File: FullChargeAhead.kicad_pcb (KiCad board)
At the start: 2 copper layers, 16 parts, among them P101 USB_OTG, P102 CONN_01X02, P103 JST_2PIN, U101 MCP73834

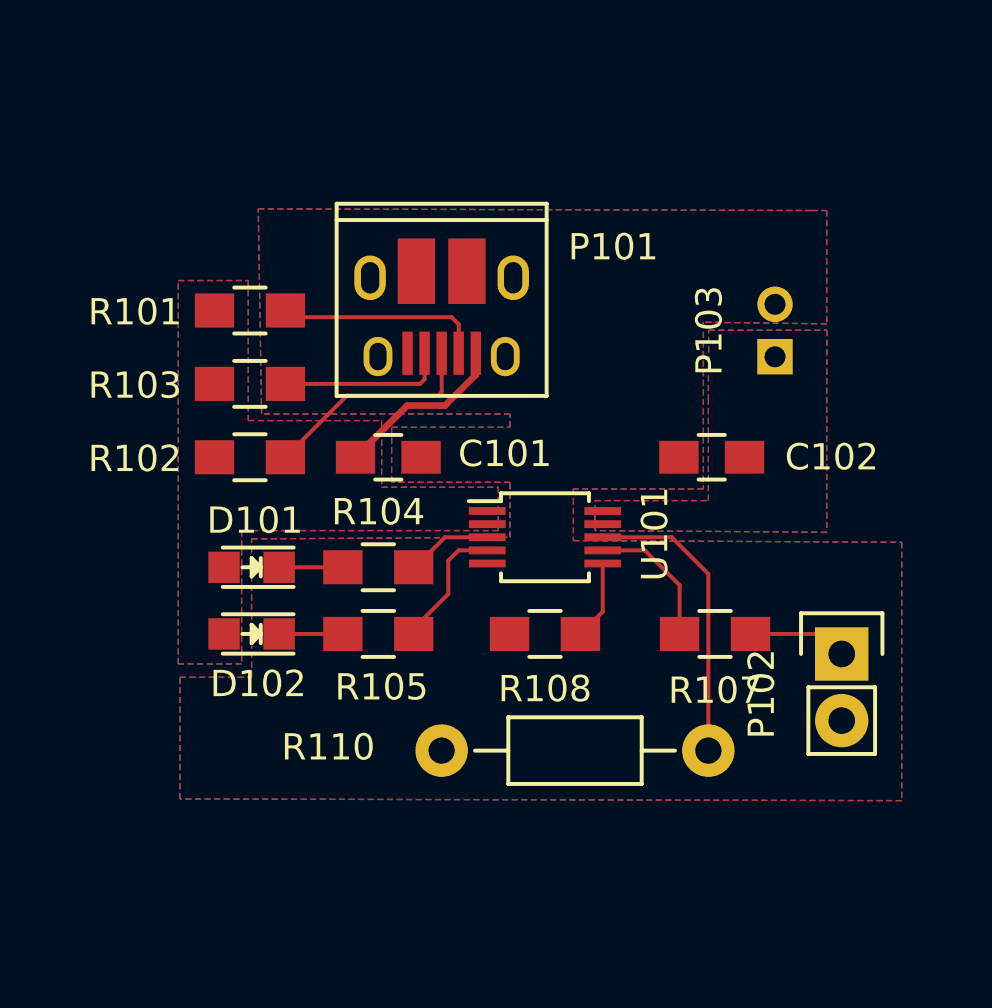
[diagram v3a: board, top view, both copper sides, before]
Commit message: new usb connector, via stiching, and gerbers
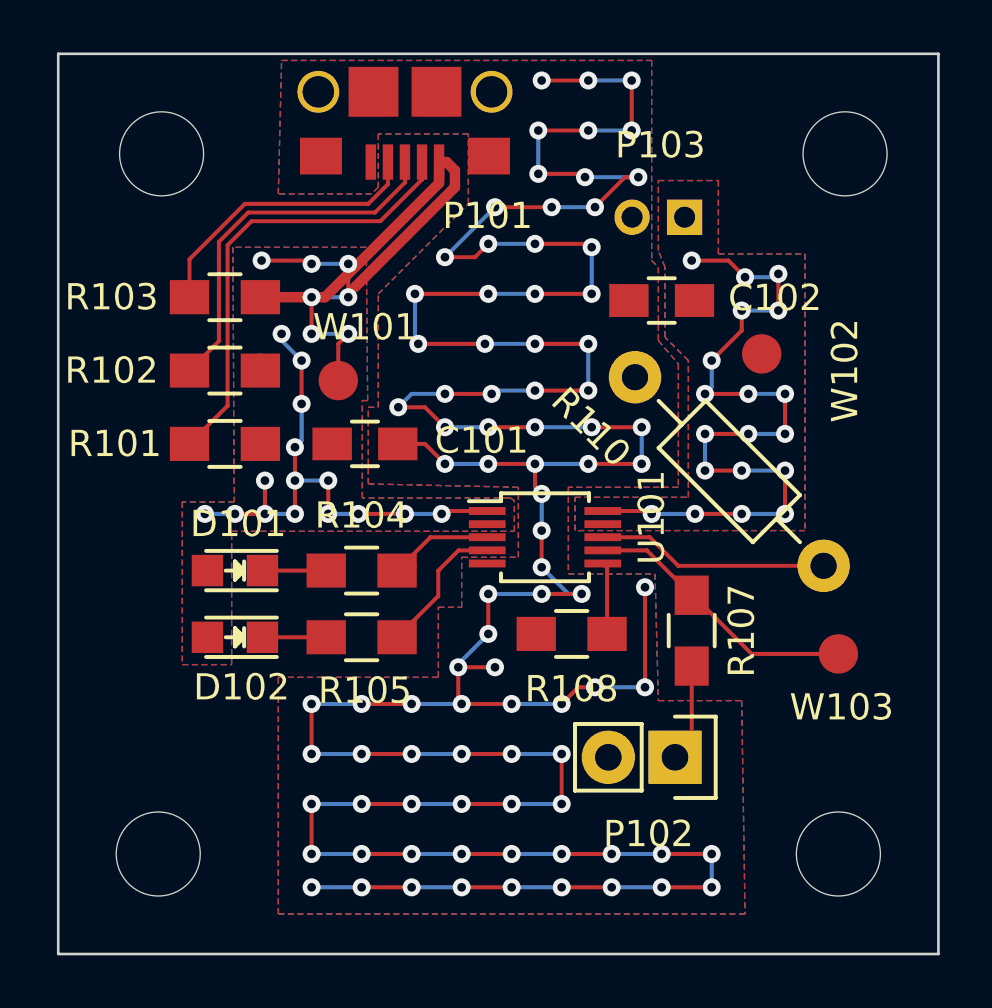
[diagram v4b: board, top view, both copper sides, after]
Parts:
- added REF**: MountingHole_3.2mm_M3, Mounting_Holes:MountingHole_3.2mm_M3, F.Cu at (164.8, 114.3)
- added REF**: MountingHole_3.2mm_M3, Mounting_Holes:MountingHole_3.2mm_M3, F.Cu at (138.9, 114.3)
- added REF**: MountingHole_3.2mm_M3, Mounting_Holes:MountingHole_3.2mm_M3, F.Cu at (139.1, 87.6)
- added REF**: MountingHole_3.2mm_M3, Mounting_Holes:MountingHole_3.2mm_M3, F.Cu at (165.1, 87.6)
- added W101: TEST_1P, Measurement_Points:Measurement_Point_Round-SMD-Pad_Small, F.Cu at (145.8, 96.3)
- added W102: TEST_1P, Measurement_Points:Measurement_Point_Round-SMD-Pad_Small, F.Cu at (161.9, 95.2)
- added W103: TEST_1P, Measurement_Points:Measurement_Point_Round-SMD-Pad_Small, F.Cu at (164.8, 106.7)
- P101: footprint FullChargeAhead:USB_Micro-B_10103594-0001LF -> FullChargeAhead:10118193
- moved R110 16.0 mm to (157.1, 96.1), turned to 315 degrees
- moved P101 8.57 mm to (148.3, 85.3)
- moved P102 7.47 mm to (158.6, 110.6), turned to 270 degrees
- moved C102 6.27 mm to (158.1, 93.2)
- moved P103 6.20 mm to (158.0, 90.0), turned to 0 degrees
- moved R101 5.17 mm to (141.5, 98.7), turned to 180 degrees
- moved R103 3.44 mm to (141.5, 93.1), turned to 180 degrees
- moved R102 3.44 mm to (141.5, 95.9), turned to 180 degrees
- moved C101 1.02 mm to (146.8, 98.7)
- moved R108 1.02 mm to (154.7, 105.9)
- moved R107 0.90 mm to (159.3, 105.8), turned to 270 degrees
- moved D101 0.65 mm to (141.9, 103.5)
- moved D102 0.65 mm to (141.9, 106.0)
- moved R104 0.65 mm to (146.7, 103.5)
- moved R105 0.65 mm to (146.7, 106.0)
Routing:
- net GND: track 0.00 -> 164.6 mm, vias 0 -> 87
- net /Vdd: track 6.70 -> 48.2 mm, vias 0 -> 22
- net /Vbat: track 0.00 -> 30.9 mm, vias 0 -> 19
- net Net-(P101-Pad2): track 7.92 -> 17.3 mm
- net Net-(P101-Pad3): track 8.46 -> 14.2 mm
- net Net-(R107-Pad1): track 5.33 -> 10.6 mm
- net Net-(P101-Pad4): track 6.37 -> 11.0 mm
- net Net-(R110-Pad2): track 11.3 -> 8.86 mm
- net Net-(R104-Pad2): track 3.27 -> 4.01 mm
- net Net-(R105-Pad2): track 4.98 -> 5.58 mm
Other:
- board outline added: 33.5 x 34.3 mm

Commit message: generated gerbers including solder stencil
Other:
- rule pad_to_mask_clearance: 0.2 -> 0
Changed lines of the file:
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@@
     (pad_size 3.2 3.2)
     (pad_drill 3.2)
-    (pad_to_mask_clearance 0.2)
+    (pad_to_mask_clearance 0)
     (aux_axis_origin 0 0)
     (visible_elements FFFFFF7F)
     (pcbplotparams
-      (layerselection 0x010f0_80000001)
+      (layerselection 0x010f8_80000001)
       (usegerberextensions true)
       (excludeedgelayer true)
